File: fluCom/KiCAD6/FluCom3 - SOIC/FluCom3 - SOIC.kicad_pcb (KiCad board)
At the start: 2 copper layers, 114 x 56.7 mm, 45 parts, among them J1 Raspberry_Pi_2_3, J2 Debug, J3 Conn_02x08_Top_Bottom, J4 DB25_Female, J5 POWER, J6 PWset, J7 12V in, J8 12V in Barrel Jack, Q1 BSS138, Q2 BSS138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

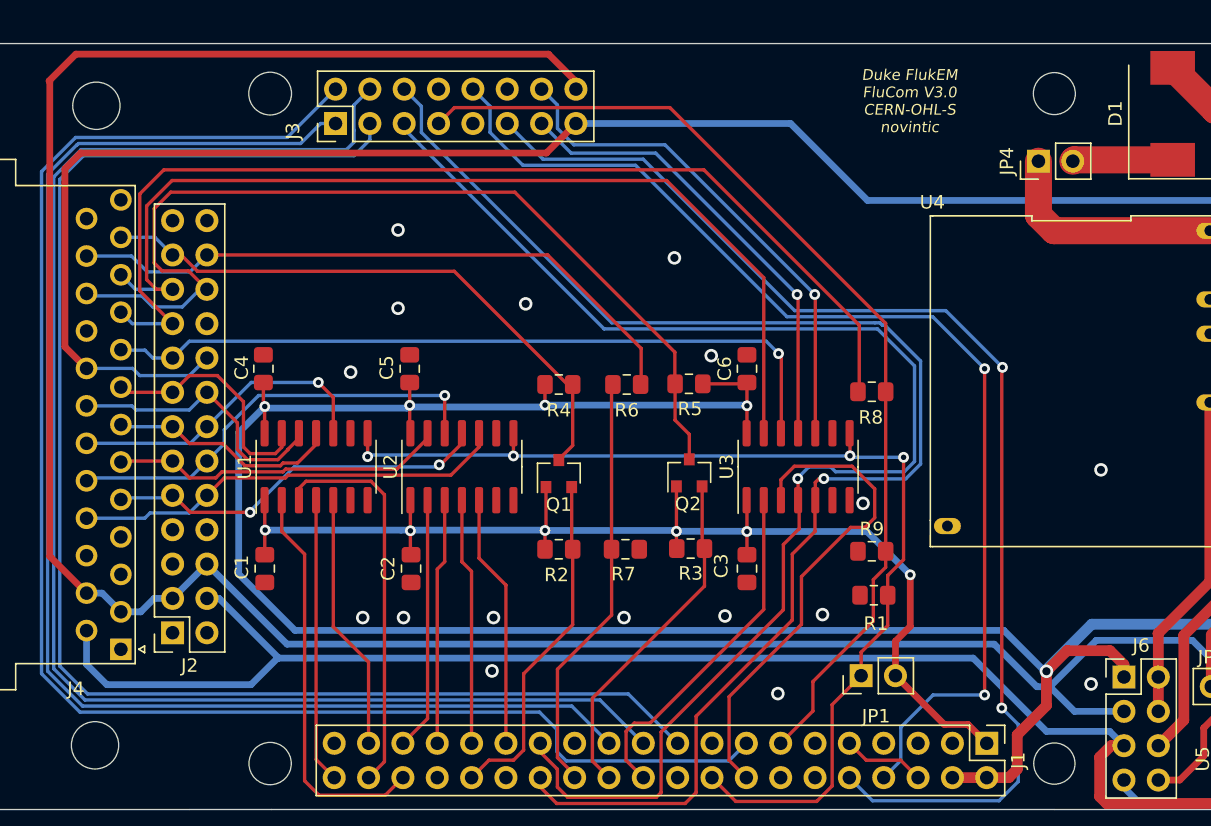
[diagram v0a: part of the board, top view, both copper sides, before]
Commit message: Add files via upload
Increased track with of +5V POD rail (should be able to provide up to 2A for larger pods like 68K)
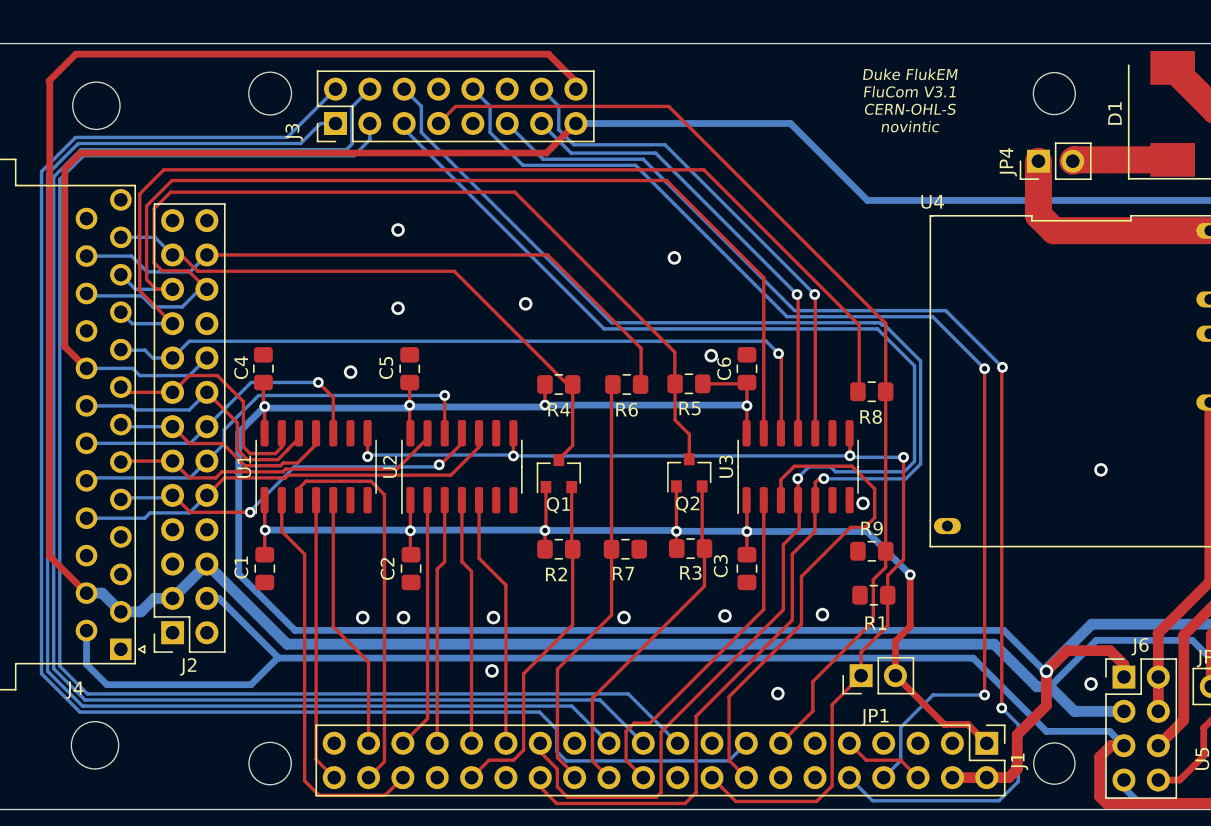
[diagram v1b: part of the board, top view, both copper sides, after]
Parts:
- R8: value 10K -> 1K!
- R9: value 20K(10K works) -> 2K!
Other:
- board text added: "Duke FlukEM FluCom V3.1 CERN-OHL-S novintic"
- board text removed: "Duke FlukEM FluCom V3.0 CERN-OHL-S novintic"
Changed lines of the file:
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@@
     (title "FluCom")
     (date "2022-04-08")
-    (rev "3.0")
+    (rev "3.1")
     (comment 1 "CERN-OHL-version-2 ")
     (comment 3 "mirko (novintic)")
@@
       (effects (font (size 1 1) (thickness 0.15)))
     )
-    (fp_text value "10K" (at 0 2.1) (layer "F.Fab")
+    (fp_text value "1K!" (at 0 2.1) (layer "F.Fab")
       (effects (font (size 1 1) (thickness 0.15)))
     )
@@
       (effects (font (size 1 1) (thickness 0.15)))
     )
-    (fp_text value "20K(10K works)" (at -9.577 2.6) (layer "F.Fab")
+    (fp_text value "2K!" (at -9.577 2.6) (layer "F.Fab")
       (effects (font (size 1 1) (thickness 0.15)))
     )
@@
   (gr_circle (center 138 87.45) (end 139.5 87.85) (layer "Edge.Cuts") (width 0.05) (fill none))
   (gr_circle (center 67.15 88.35) (end 67.15 86.6) (layer "Edge.Cuts") (width 0.05) (fill none))
-  (gr_text "Duke FlukEM \nFluCom V3.0 \nCERN-OHL-S\nnovintic" (at 127.3 88) (layer "F.SilkS")
+  (gr_text "Duke FlukEM \nFluCom V3.1\nCERN-OHL-S\nnovintic" (at 127.3 88) (layer "F.SilkS")
     (effects (font (size 0.8 0.8) (thickness 0.1) italic))
   )
@@
   (segment (start 126.8476 114.3508) (end 123.000911 114.3508) (width 0.249987) (layer "B.Cu") (net 23))
   (segment (start 97.9932 114.2492) (end 97.923495 114.179495) (width 0.249987) (layer "B.Cu") (net 23))
+  (segment (start 63.992594 129.980426) (end 63.992595 93.613721) (width 0.249987) (layer "B.Cu") (net 24))
+  (segment (start 104.398606 132.298606) (end 66.310773 132.298605) (width 0.249987) (layer "B.Cu") (net 24))
+  (segment (start 86.05 91.1912) (end 86.05 88.448) (width 0.249987) (layer "B.Cu") (net 24))
+  (segment (start 63.992595 93.613721) (end 66.013917 91.592399) (width 0.249987) (layer "B.Cu") (net 24))
+  (segment (start 107.6 135.5) (end 104.398606 132.298606) (width 0.249987) (layer "B.Cu") (net 24))
+  (segment (start 85.648801 91.592399) (end 86.05 91.1912) (width 0.249987) (layer "B.Cu") (net 24))
+  (segment (start 66.013917 91.592399) (end 85.648801 91.592399) (width 0.249987) (layer "B.Cu") (net 24))
   (segment (start 66.310773 132.298605) (end 63.992594 129.980426) (width 0.249987) (layer "B.Cu") (net 24))
-  (segment (start 63.992594 129.980426) (end 63.992595 93.613721) (width 0.249987) (layer "B.Cu") (net 24))
-  (segment (start 104.398606 132.298606) (end 107.6 135.5) (width 0.249987) (layer "B.Cu") (net 24))
-  (segment (start 86.201496 88.296504) (end 87.376 87.122) (width 0.249987) (layer "B.Cu") (net 24))
-  (segment (start 63.992595 93.613721) (end 66.013917 91.592399) (width 0.249987) (layer "B.Cu") (net 24))
-  (segment (start 85.648801 91.592399) (end 86.2076 91.0336) (width 0.249987) (layer "B.Cu") (net 24))
-  (segment (start 86.2076 91.0336) (end 86.2076 90.154601) (width 0.249987) (layer "B.Cu") (net 24))
-  (segment (start 86.2076 90.154601) (end 86.201496 90.148497) (width 0.249987) (layer "B.Cu") (net 24))
-  (segment (start 104.398606 132.298606) (end 66.310773 132.298605) (width 0.249987) (layer "B.Cu") (net 24))
-  (segment (start 66.013917 91.592399) (end 85.648801 91.592399) (width 0.249987) (layer "B.Cu") (net 24))
-  (segment (start 86.201496 90.148497) (end 86.201496 88.296504) (width 0.249987) (layer "B.Cu") (net 24))
+  (segment (start 86.05 88.448) (end 87.376 87.122) (width 0.249987) (layer "B.Cu") (net 24))
   (segment (start 106.3244 136.7644) (end 107.6 138.04) (width 0.25) (layer "F.Cu") (net 25))
   (segment (start 116.508 125.6048) (end 108.1024 134.0104) (width 0.25) (layer "F.Cu") (net 25))
@@
   (segment (start 159.175 116.2118) (end 157.8356 117.5512) (width 0.8) (layer "F.Cu") (net 41))
   (segment (start 141.097 127.889) (end 137.668 131.318) (width 0.5) (layer "B.Cu") (net 41))
-  (segment (start 81.2484 128.1684) (end 75.325 122.245) (width 0.5) (layer "B.Cu") (net 41))
-  (segment (start 137.668 131.318) (end 139.49 133.14) (width 0.5) (layer "B.Cu") (net 41))
-  (segment (start 133.5532 128.1684) (end 81.2484 128.1684) (width 0.5) (layer "B.Cu") (net 41))
-  (segment (start 71.43 124.785) (end 72.785 124.785) (width 0.5) (layer "B.Cu") (net 41))
-  (segment (start 75.325 122.245) (end 72.785 124.785) (width 0.5) (layer "B.Cu") (net 41))
-  (segment (start 137.668 131.318) (end 136.7028 131.318) (width 0.5) (layer "B.Cu") (net 41))
+  (segment (start 81.2484 128.1684) (end 75.325 122.245) (width 0.8) (layer "B.Cu") (net 41))
+  (segment (start 137.668 131.318) (end 139.49 133.14) (width 0.8) (layer "B.Cu") (net 41))
+  (segment (start 133.5532 128.1684) (end 81.2484 128.1684) (width 0.8) (layer "B.Cu") (net 41))
+  (segment (start 71.43 124.785) (end 72.785 124.785) (width 0.8) (layer "B.Cu") (net 41))
+  (segment (start 75.325 122.245) (end 72.785 124.785) (width 0.8) (layer "B.Cu") (net 41))
+  (segment (start 137.668 131.318) (end 136.7028 131.318) (width 0.8) (layer "B.Cu") (net 41))
   (segment (start 148.209 127.889) (end 141.097 127.889) (width 0.5) (layer "B.Cu") (net 41))
-  (segment (start 67.576 124.395) (end 68.961 125.78) (width 0.5) (layer "B.Cu") (net 41))
-  (segment (start 136.7028 131.318) (end 133.5532 128.1684) (width 0.5) (layer "B.Cu") (net 41))
-  (segment (start 70.435 125.78) (end 71.43 124.785) (width 0.5) (layer "B.Cu") (net 41))
-  (segment (start 139.49 133.14) (end 143.15 133.14) (width 0.5) (layer "B.Cu") (net 41))
+  (segment (start 67.576 124.395) (end 68.961 125.78) (width 0.8) (layer "B.Cu") (net 41))
+  (segment (start 136.7028 131.318) (end 133.5532 128.1684) (width 0.8) (layer "B.Cu") (net 41))
+  (segment (start 70.435 125.78) (end 71.43 124.785) (width 0.8) (layer "B.Cu") (net 41))
+  (segment (start 139.49 133.14) (end 143.15 133.14) (width 0.8) (layer "B.Cu") (net 41))
   (segment (start 149.606 131.3) (end 149.606 129.286) (width 0.5) (layer "B.Cu") (net 41))
-  (segment (start 68.961 125.78) (end 70.435 125.78) (width 0.5) (layer "B.Cu") (net 41))
-  (segment (start 66.421 124.395) (end 67.576 124.395) (width 0.5) (layer "B.Cu") (net 41))
+  (segment (start 68.961 125.78) (end 70.435 125.78) (width 0.8) (layer "B.Cu") (net 41))
+  (segment (start 66.421 124.395) (end 67.576 124.395) (width 0.8) (layer "B.Cu") (net 41))
   (segment (start 149.606 129.286) (end 148.209 127.889) (width 0.5) (layer "B.Cu") (net 41))
   (segment (start 74.097738 118.420034) (end 78.5227 118.420034) (width 0.25) (layer "F.Cu") (net 42))
@@
   (segment (start 125.525 121.3) (end 125.525 122.4806) (width 0.25) (layer "F.Cu") (net 60))
   (segment (start 125.525 104.443) (end 125.525 109.5) (width 0.249987) (layer "F.Cu") (net 60))
-  (segment (start 92.456 89.662) (end 93.630504 88.487496) (width 0.249987) (layer "F.Cu") (net 60))
+  (segment (start 93.718 88.4) (end 109.482 88.4) (width 0.249987) (layer "F.Cu") (net 60))
   (segment (start 125.525 109.5) (end 125.525 121.3) (width 0.249987) (layer "F.Cu") (net 60))
-  (segment (start 109.569496 88.487496) (end 125.525 104.443) (width 0.249987) (layer "F.Cu") (net 60))
   (segment (start 124.6124 123.3932) (end 124.6124 126.4666) (width 0.25) (layer "F.Cu") (net 60))
+  (segment (start 109.482 88.4) (end 125.525 104.443) (width 0.249987) (layer "F.Cu") (net 60))
   (segment (start 124.6124 126.4666) (end 120.142 130.937) (width 0.25) (layer "F.Cu") (net 60))
-  (segment (start 93.630504 88.487496) (end 109.569496 88.487496) (width 0.249987) (layer "F.Cu") (net 60))
   (segment (start 120.142 133.118) (end 117.76 135.5) (width 0.25) (layer "F.Cu") (net 60))
   (segment (start 125.525 122.4806) (end 124.6124 123.3932) (width 0.25) (layer "F.Cu") (net 60))
+  (segment (start 92.456 89.662) (end 93.718 88.4) (width 0.249987) (layer "F.Cu") (net 60))
   (segment (start 65.82773 91.142902) (end 82.25511 91.142903) (width 0.249987) (layer "B.Cu") (net 67))
   (segment (start 65.741535 91.229097) (end 65.82773 91.142902) (width 0.249987) (layer "B.Cu") (net 67))
@@
   (segment (start 120.318 112.572) (end 120.318 102.348932) (width 0.249987) (layer "F.Cu") (net 71))
   (via (at 120.278444 102.309376) (size 0.8) (drill 0.4) (layers "F.Cu" "B.Cu") (net 71))
+  (segment (start 101.35 88.396) (end 101.35 90.1232) (width 0.249987) (layer "B.Cu") (net 71))
   (segment (start 109.205868 91.2368) (end 120.278444 102.309376) (width 0.249987) (layer "B.Cu") (net 71))
-  (segment (start 101.250504 88.296504) (end 101.250504 90.023704) (width 0.249987) (layer "B.Cu") (net 71))
-  (segment (start 101.250504 90.023704) (end 102.4636 91.2368) (width 0.249987) (layer "B.Cu") (net 71))
   (segment (start 102.4636 91.2368) (end 109.205868 91.2368) (width 0.249987) (layer "B.Cu") (net 71))
-  (segment (start 100.076 87.122) (end 101.250504 88.296504) (width 0.249987) (layer "B.Cu") (net 71))
+  (segment (start 101.35 90.1232) (end 102.4636 91.2368) (width 0.249987) (layer "B.Cu") (net 71))
+  (segment (start 100.076 87.122) (end 101.35 88.396) (width 0.249987) (layer "B.Cu") (net 71))
   (zone (net 2) (net_name "GND") (layer "F.Cu") (hatch edge 0.508)
     (connect_pads (clearance 0.508))
